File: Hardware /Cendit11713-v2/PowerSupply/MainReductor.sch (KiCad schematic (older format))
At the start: 39 parts

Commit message: En CenditLab + Cendit11713: commit masivo
 - Trabajo en clases + fxml UI
 - Trabajo en main board option 2 + correccion tarjeta expansor Viking
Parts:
- removed D? (x7): D_Schottky, symbol D_Schottky
- removed D?: D, symbol D
- removed D?: D_Zener, symbol D_Zener
- removed Q? (x2): NPN, symbol NPN
- removed R? (x5): R_Small, symbol R_Small
- removed R? (x2): RSENSE, symbol R_Small
- removed RV?: POT, symbol POT
- removed T? (x3): N-MOSFET, symbol TRANSISTOR-N-MOSFET-ENHANCEMENT_RevE_Date15jun2010
- removed TR?: XFRMR_PA2653NL, symbol XFRMR_PA2653NL
- added C? (x3): C, symbol C
- added C? (x2): C_Small, symbol C_Small
- added D?: MBRD10200CT, symbol D_Schottky_x2_KCom_AKA
- added D? (x3): DURD560A, symbol D_Schottky_AKA
- added D? (x2): D_Small, symbol D_Small
- added JP? (x2): Jumper_NC_Dual, symbol Jumper_NC_Dual
- added JP? (x2): XCHG, symbol Jumper_NO_Small
- added L?: L_Core_Ferrite, symbol L_Core_Ferrite
- added Q? (x2): 13003, symbol Q_NPN_BCE
- added Q?: Q_NPN_BCE, symbol Q_NPN_BCE
- added R? (x9): R, symbol R
- added R? (x2): R_Small, symbol R_Small
- added RV? (x2): POT, symbol POT
- added T1: PA1297NL, symbol PA1297NL
- D?: value D_Zener -> 20V@1W
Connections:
- net labels added: DEAD_TIME, Earth, I_SENSE, I_SHORT, SNUBBER, TR_PRI_N, TR_PRI_P, TR_SEC_N, TR_SEC_P, TR_SEN_N, TR_SEN_P, VCC, VFBK, VIN_1_N, VREF_5V, V_SENSE, V_SET
- net labels removed: COIL_N, COIL_P, VFBCK, VREF
- wire segments 74 -> 130
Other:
- moved on the sheet: C?, D?, R?, U?

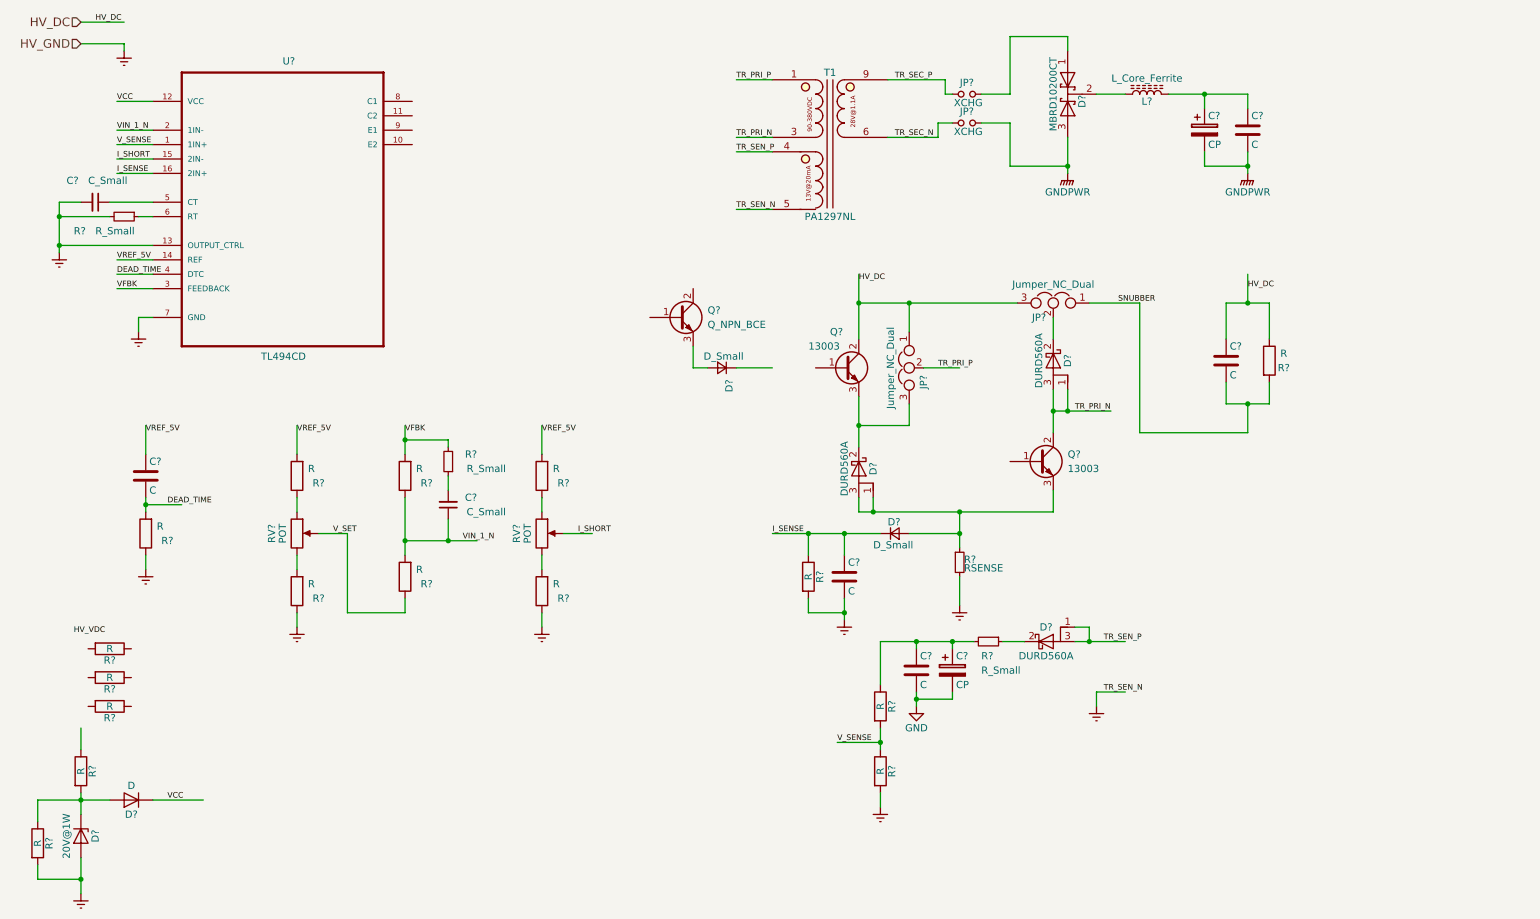
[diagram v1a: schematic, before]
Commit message: Trabajo en Cendit11713 + respaldo de lo hecho hasta hoy
  - Segunda etapa regulador reductor conmutado + LDO
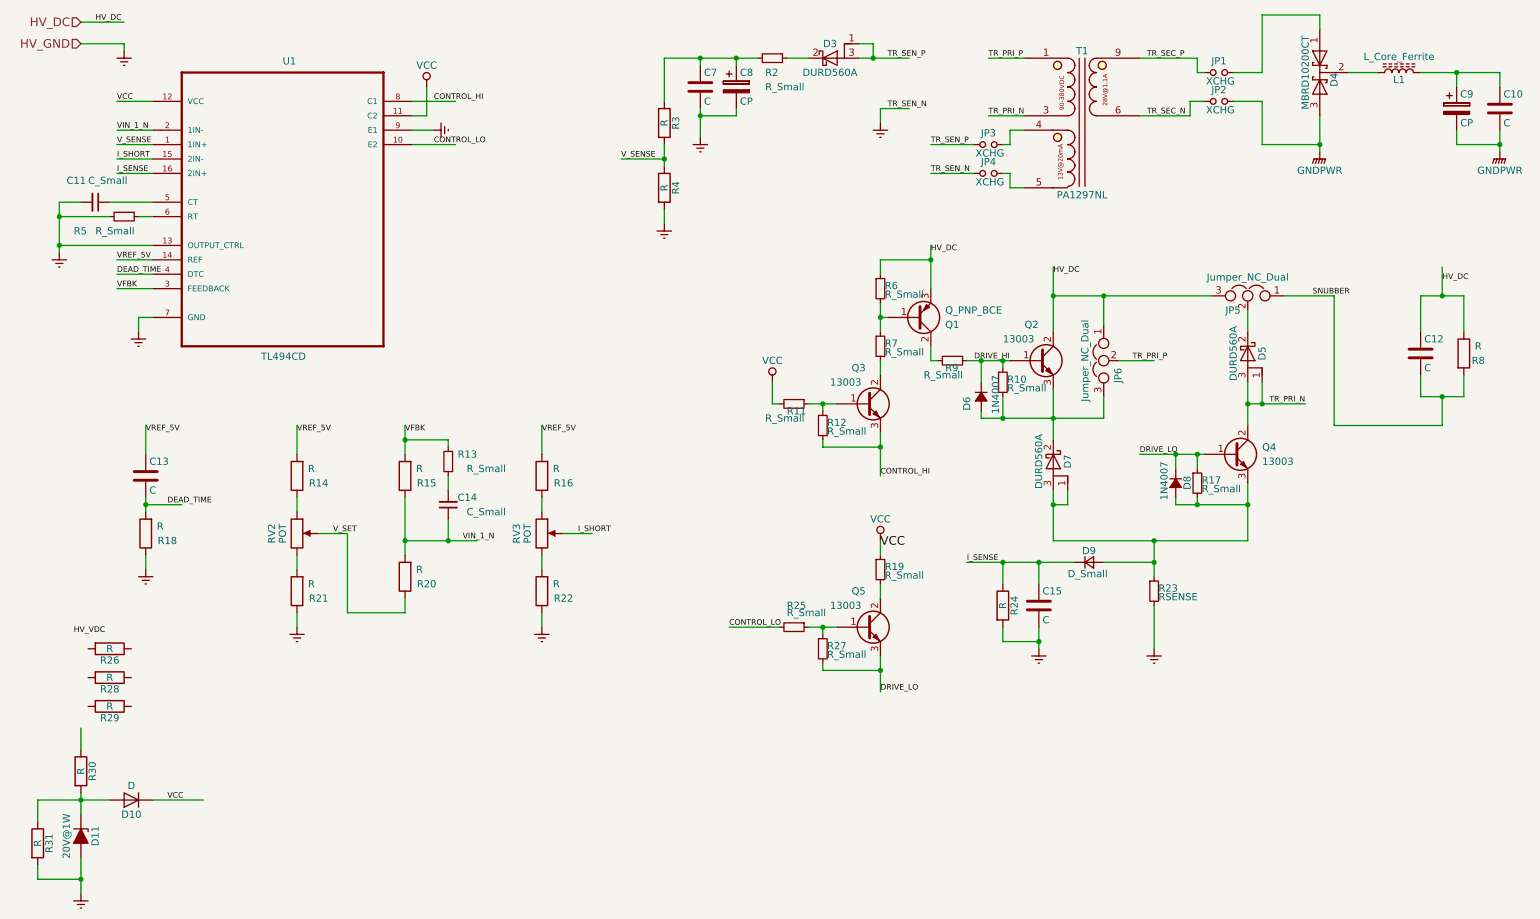
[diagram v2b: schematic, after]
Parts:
- removed D?: 20V@1W, symbol D_Zener
- removed D?: D_Small, symbol D_Small
- removed Q?: Q_NPN_BCE, symbol Q_NPN_BCE
- added D11: 20V@1W, symbol D_Zener_ALT
- added D6, D8: 1N4007, symbol D_Small_ALT
- added JP3, JP4: XCHG, symbol Jumper_NO_Small
- added Q1: Q_PNP_BCE, symbol Q_PNP_BCE
- added Q3, Q5: 13003, symbol Q_NPN_BCE
- added R10, R11, R12, R17, R19, R25, R27, R6, R7, R9: R_Small, symbol R_Small
- gave numbers to parts that had none: 45
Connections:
- net labels added: CONTROL_HI, CONTROL_LO, DRIVE_HI, DRIVE_LO
- net labels removed: GND
- wire segments 130 -> 173
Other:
- moved on the sheet: C10, C12, C15, C7, C8, C9, D3, D4, D5, D7, D9, JP1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
